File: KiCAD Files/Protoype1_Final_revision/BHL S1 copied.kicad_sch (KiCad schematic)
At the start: 94 parts, among them IC1 NUP2105LT1G, IC2 NUP2105LT1G, IC3 IR2136STRPBF, J1 39-30-1042, J2 Conn_01x03_Pin, J3 Conn_01x03_Pin, J4 39-30-1042, Q1 CSD19502Q5B, Q2 CSD19502Q5B, Q3 CSD19502Q5B, Q4 CSD19502Q5B, Q5 CSD19502Q5B, Q7 CSD19502Q5B, U1 ME6211C30M5, U2 SPX3819M5-L-5-0, U3 Solder Pad, U5 STM32G431CBU6, Y1 8MHz

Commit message: Footprint and 3d model updated, PCB updated
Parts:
- removed C29: 10uF/35V, Capacitor_SMD:C_0805_2012Metric_Pad1.18x1.45mm_HandSolder, symbol Device:C
- removed IC3: IR2136STRPBF, Footprint for BHL S1:3PHASE_GATE_DRIVER, symbol BHLS1_3PHASE_DRIVER:IR2136STRPBF
- added C5: 10uF/35V, Capacitor_SMD:C_0805_2012Metric_Pad1.18x1.45mm_HandSolder, symbol Device:C
- added IC4: FD6288Q, Footprint for BHL S1:QFN50P400X400X90-25N-D_Gatedriver1, symbol BHLS1_FD6288Q_Gatedriver1$:FD6288Q
- ME3116: footprint Footprint for BHL S1:ME3116AM6G_Regulator -> Footprint for BHL S1:SOT95P270X145-6N_ME3116
- U5: footprint Footprint for BHL S1:QFN50P700X700X60-49N -> Footprint for BHL S1:QFN50P700X700X60-49N_STM32
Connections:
- net GH_A: now also IC4.19 (HO1)
- net GH_B: now also IC4.16 (HO2)
- net GH_C: now also IC4.13 (HO3)
- net GL_A: now also IC4.11 (LO1)
- net GL_B: now also IC4.10 (LO2)
- net GL_C: now also IC4.9 (LO3)
- net GND: now also C5.2, IC4.25 (EP), IC4.6 (COM)
- net HIN1: now also IC4.22 (HIN1)
- net HIN2: now also IC4.23 (HIN2)
- net HIN3: now also IC4.24 (HIN3)
- net LIN1: now also IC4.1 (LIN1)
- net LIN2: now also IC4.2 (LIN2)
- net LIN3: now also IC4.3 (LIN3)
- net SH_A: now also IC4.18 (VS1)
- net SH_B: now also IC4.15 (VS2)
- net SH_C: now also IC4.12 (VS3)
- net VB1: now also IC4.20 (VB1)
- net VB2: now also IC4.17 (VB2)
- net VB3: now also IC4.14 (VB3)
- net VCC_12V: now also C5.1, IC4.4 (VCC)
- no-connect marks 27 -> 24

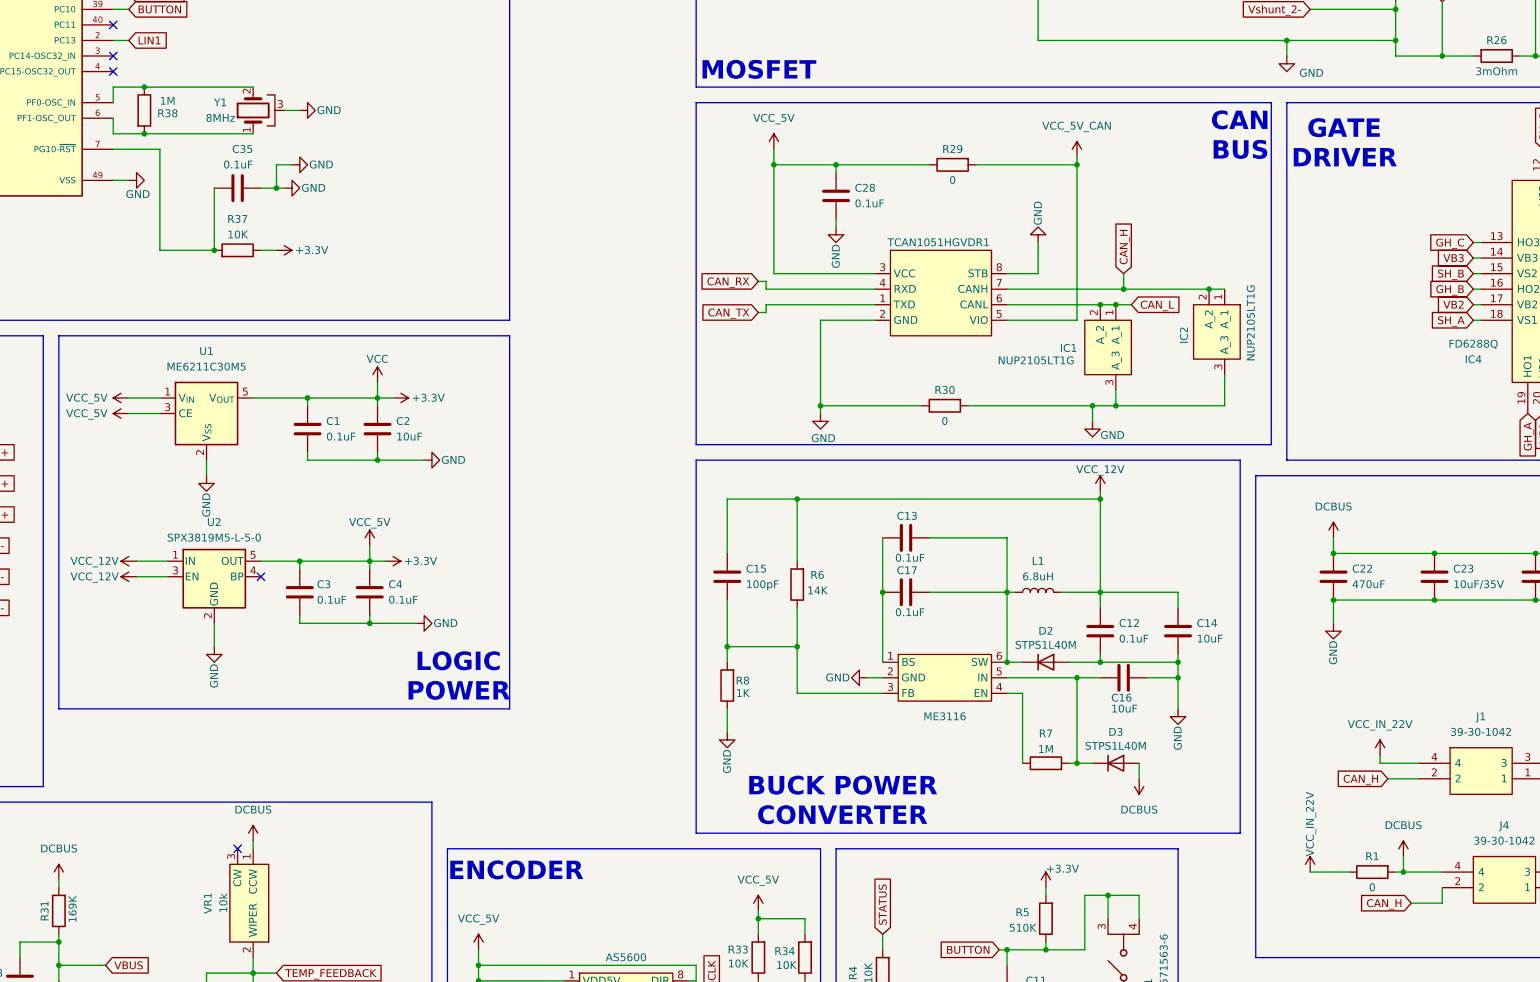
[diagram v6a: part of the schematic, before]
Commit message: fixed some errors
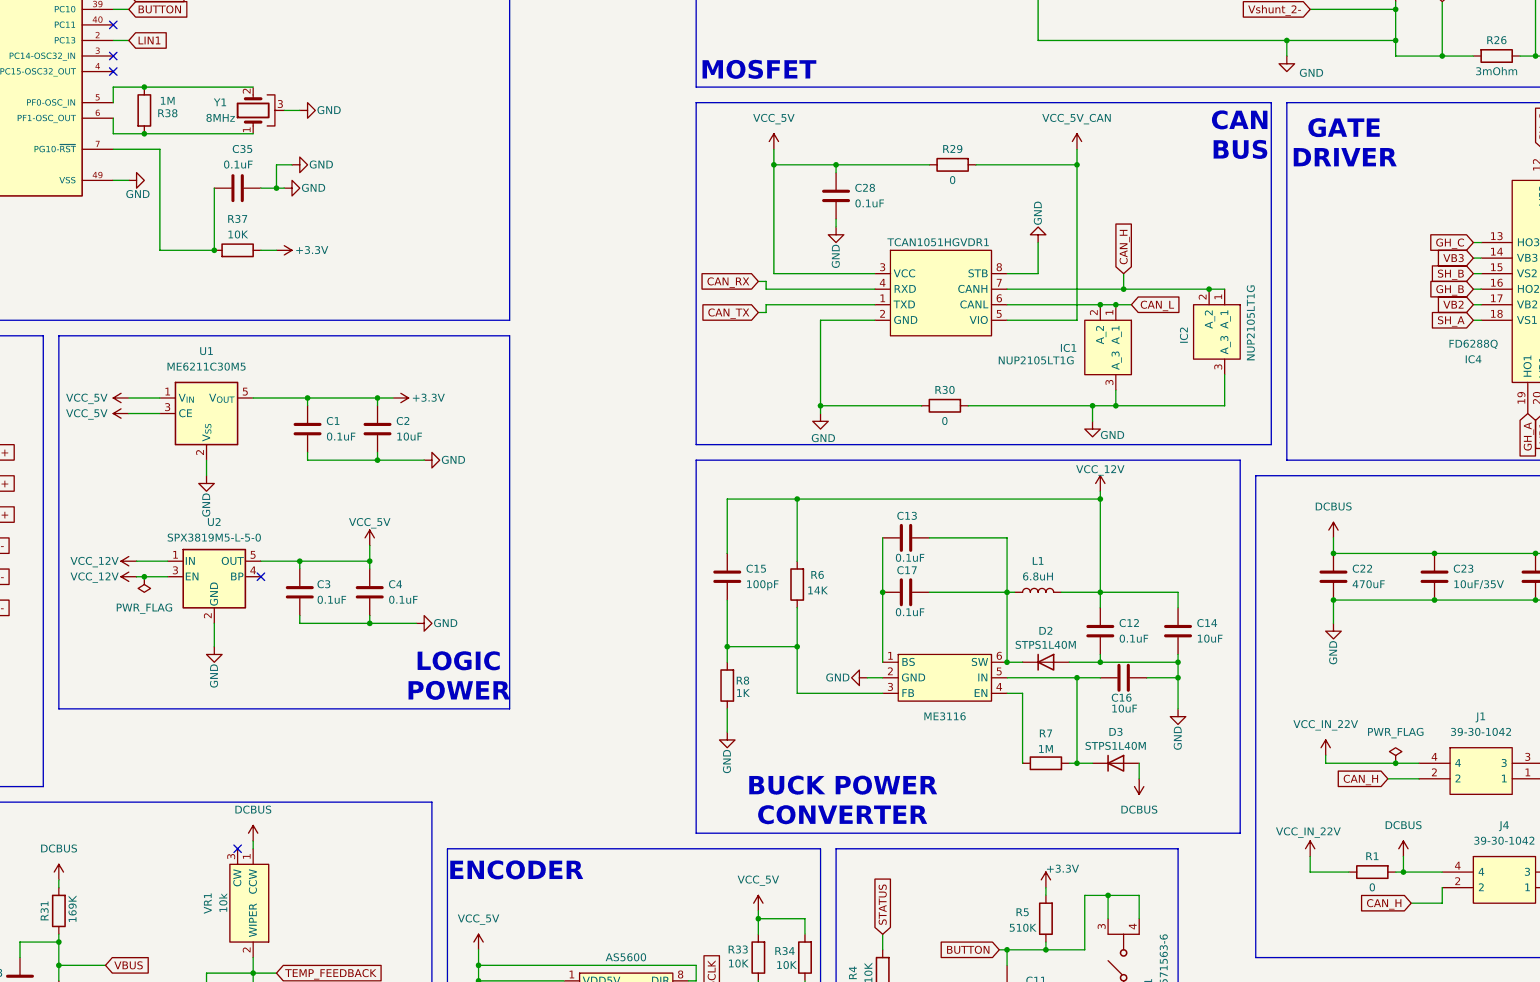
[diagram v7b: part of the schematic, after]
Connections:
- net +3.3V: no longer AS5600.1 (VDD5V), AS5600.8 (DIR), C28.1, C3.1, C33.1, C4.1, R29.1, R33.2, R34.2, TCAN1051HGVDR1.3 (VCC), U1.1 (V_{IN}), U1.3 (CE), U2.5 (OUT)
- new net VCC_5V: AS5600.1 (VDD5V), AS5600.8 (DIR), C28.1, C3.1, C33.1, C4.1, R29.1, R33.2, R34.2, TCAN1051HGVDR1.3 (VCC), U1.1 (V_{IN}), U1.3 (CE), U2.5 (OUT)

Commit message: Attempted to fix some errors
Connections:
- net VCC_IN_22V is gone; now on net DCBUS: J1.4, R1.1
- net DCBUS: no longer J4.4, R1.2
- net VCC_5V_CAN: no longer names the net of R29.2, TCAN1051HGVDR1.5 (VIO)
- new net: J4.4, R1.2
